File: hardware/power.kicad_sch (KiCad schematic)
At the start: 20 parts, among them Q1 TK3P80E,RQ, U1 LT8316EFE

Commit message: Improve the layout
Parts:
- removed D3: ${SIM.PARAMS}, Diode_SMD:D_SOD-323, symbol Simulation_SPICE:DIODE
- added C9: DNP, Capacitor_SMD:CP_Elec_6.3x5.4, symbol Device:C_Polarized_Small
- added D3: CMDSH2-3, Diode_SMD:D_SOD-323, symbol Diode:US1K
- added TP10: LT_VIN, TestPoint:TestPoint_Pad_D1.0mm, symbol Connector:TestPoint
- added TP11: LT_GATE, TestPoint:TestPoint_Pad_D1.0mm, symbol Connector:TestPoint
- added TP12: LT_SENSE, TestPoint:TestPoint_Pad_D1.0mm, symbol Connector:TestPoint
- added TP13: LT_VOUT, TestPoint:TestPoint_Pad_D1.0mm, symbol Connector:TestPoint
- added TP4: LT_D3, TestPoint:TestPoint_Pad_D1.0mm, symbol Connector:TestPoint
- added TP5: LT_VC, TestPoint:TestPoint_Pad_D1.0mm, symbol Connector:TestPoint
- added TP6: LT_BIAS, TestPoint:TestPoint_Pad_D1.0mm, symbol Connector:TestPoint
- added TP7: LT_FB, TestPoint:TestPoint_Pad_D1.0mm, symbol Connector:TestPoint
- added TP8: LT_GND, TestPoint:TestPoint_Pad_D1.0mm, symbol Connector:TestPoint
- added TP9: LT_DCM, TestPoint:TestPoint_Pad_D1.0mm, symbol Connector:TestPoint
- C1: renamed from C3; value 10uF -> 10u
- C2: renamed from C4; value 100nF -> 100n
- C3: renamed from C5; value 100nF -> 100n
- C4: renamed from C1; value 0.1uF -> 100n
- C5: renamed from C2; value 10pF -> 10p
- C6, C7, C8: value 47uF -> 47u
- D4: value D_Zener 10V -> 10V
- L1: value 1mH -> 1m; footprint Inductor_SMD:L_Wuerth_WE-PD2-Typ-MS -> Local_Library:WurthElektronikInductor_7687714102
- Q1: value TK3P80E,RQ -> TK3P80ERQ
- R12: value 21.5kR -> 21k5
- R13: value 2.49kR -> 2k49
- R14: value 22.1kR -> 22k1
- R15: renamed from R11; value 10kR -> 10k
- R16: renamed from R15; value 220mR -> 220m
- U2: renamed from U1; symbol Library_indicator:LT8316EFE -> LT8316EFE:LT8316EFE_1
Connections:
- net +12V: now also C9.1, TP13.1
- net GND: now also C9.2
- net at R14.2, U2.13 (VC): now also TP5.1
- net at D4.2 (A), U2.1 (VIN), U2.2 (VIN)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: now also TP10.1
- net at R15.2, U2.10 (DCM): now also TP9.1
- net at R12.1, R13.2, U2.12 (FB): now also TP7.1
- net at C1.2, C2.2, C3.2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: now also TP8.1
- net at C1.1, U2.17 (EN/UVLO), U2.8 (INTVCC)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: now also D3.1 (K), TP6.1
- net at Q1.3 (S), R16.2, U2.18 (SENSE): now also TP12.1
- net at Q1.1 (G), U2.19 (GATE): now also TP11.1
- net at D2.1 (K), R12.2: now also D3.2 (A), TP4.1
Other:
- note removed: "we can change resistor values, but the voltage on fb2 should be 1.22V"
- company: (none) -> H. Fedarovich
- title: (none) -> Power Converter
- moved on the sheet: C1, C2, C3, C4, C5, C6, C7, C8, D2, D4, D5, L1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

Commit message: Use a transistor to drive the LED
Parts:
- renumbered C9 to C10, C1 to C2, C2 to C3, C3 to C4, C4 to C5, C5 to C6, C6 to C7, C7 to C8, C8 to C9, Q1 to Q2, R12 to R13, R13 to R14, R14 to R15, R15 to R16, R16 to R17

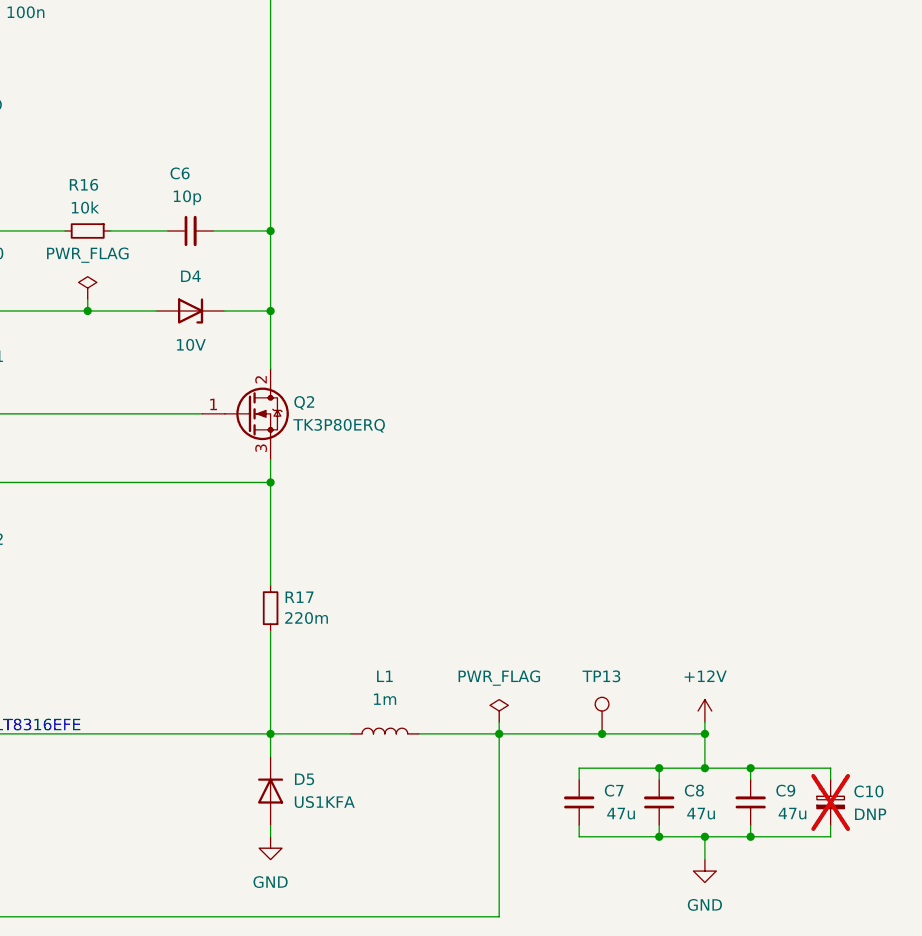
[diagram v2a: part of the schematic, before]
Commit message: Update component values
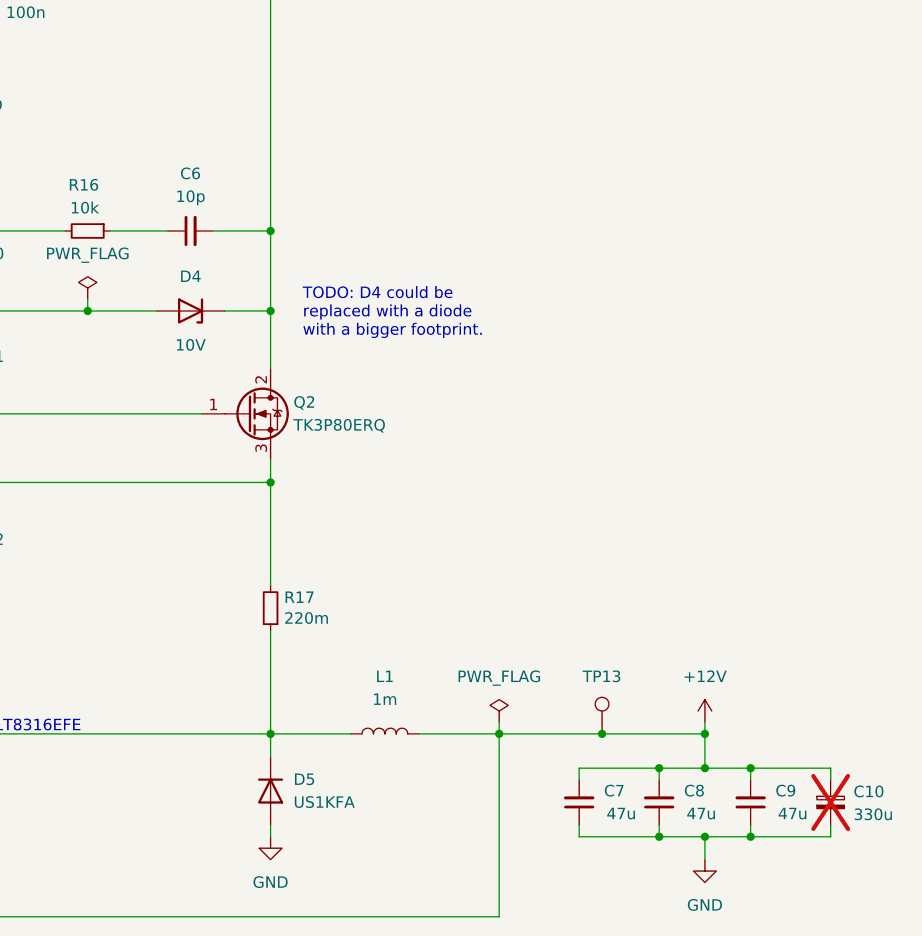
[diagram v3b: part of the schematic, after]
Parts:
- C10: value DNP -> 330u
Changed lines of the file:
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@@
     )
+  )
+  (text_box "TODO: D4 could be replaced with a diode with a bigger footprint."
+    (at 204.47 83.82 0) (size 25.4 8.89)
+    (stroke (width -0.0001) (type default))
+    (fill (type none))
+    (effects (font (size 1.27 1.27)) (justify left top))
   )
   (text "GND_LT8316EFE" (at 166.37 134.62 0)
@@
     (in_bom yes) (on_board yes) (dnp no)
     (property "Reference" "C6" (at 193.04 72.39 90)
-      (effects (font (size 1.27 1.27)) (justify left))
-    )
-    (property "Value" "10p" (at 194.31 74.93 90)
-      (effects (font (size 1.27 1.27)) (justify left))
+      (effects (font (size 1.27 1.27)))
+    )
+    (property "Value" "10p" (at 193.04 74.93 90)
+      (effects (font (size 1.27 1.27)))
     )
     (property "Footprint" "Capacitor_SMD:C_1206_3216Metric" (at 193.04 78.74 0)
@@
       (effects (font (size 1.27 1.27)) (justify left))
     )
-    (property "Value" "DNP" (at 266.7 143.5989 0)
-      (effects (font (size 1.27 1.27)) (justify left))
-    )
+    (property "Value" "330u" (at 266.7 143.5989 0)
+      (effects (font (size 1.27 1.27)) (justify left))
+    )
